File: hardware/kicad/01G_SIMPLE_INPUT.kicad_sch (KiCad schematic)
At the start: 2 parts

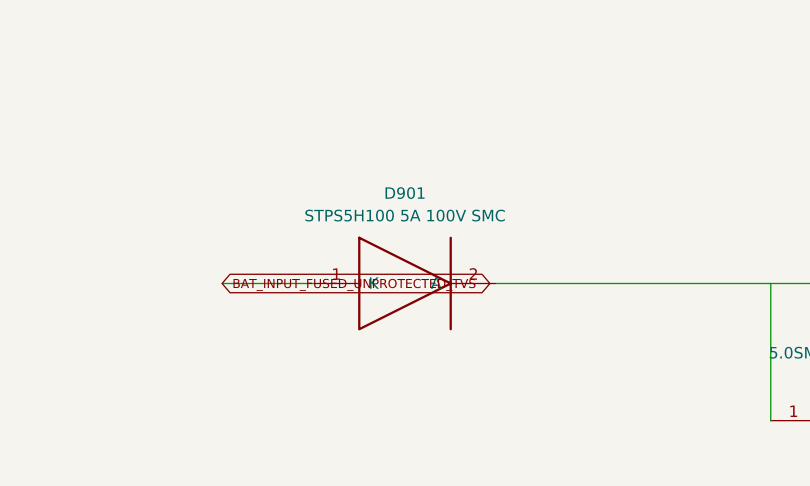
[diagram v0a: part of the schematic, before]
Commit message: fix(input): rotate series rectifier so BAT feeds anode and VIN is cathode
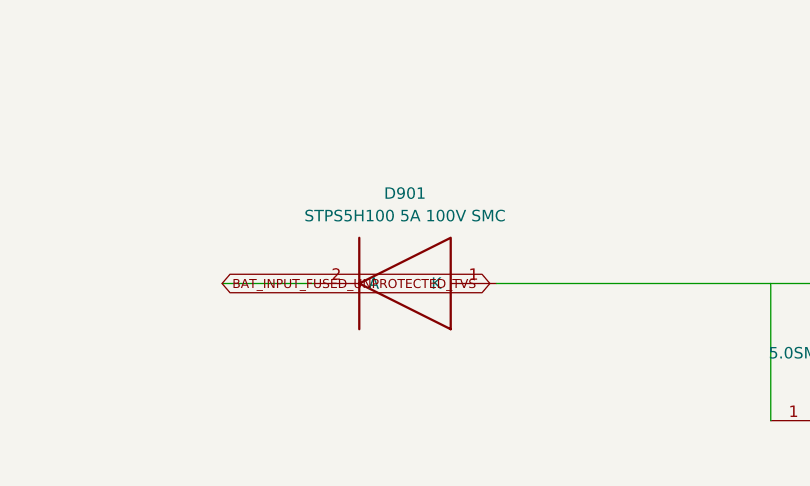
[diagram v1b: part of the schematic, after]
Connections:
- net BAT_INPUT_FUSED_UNPROTECTED_TVS: now also D901.2 (A); no longer D901.1 (K)
- net HV_PROTECTED_AFTER_EFUSE: now also D901.1 (K); no longer D901.2 (A)
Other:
- moved on the sheet: D901

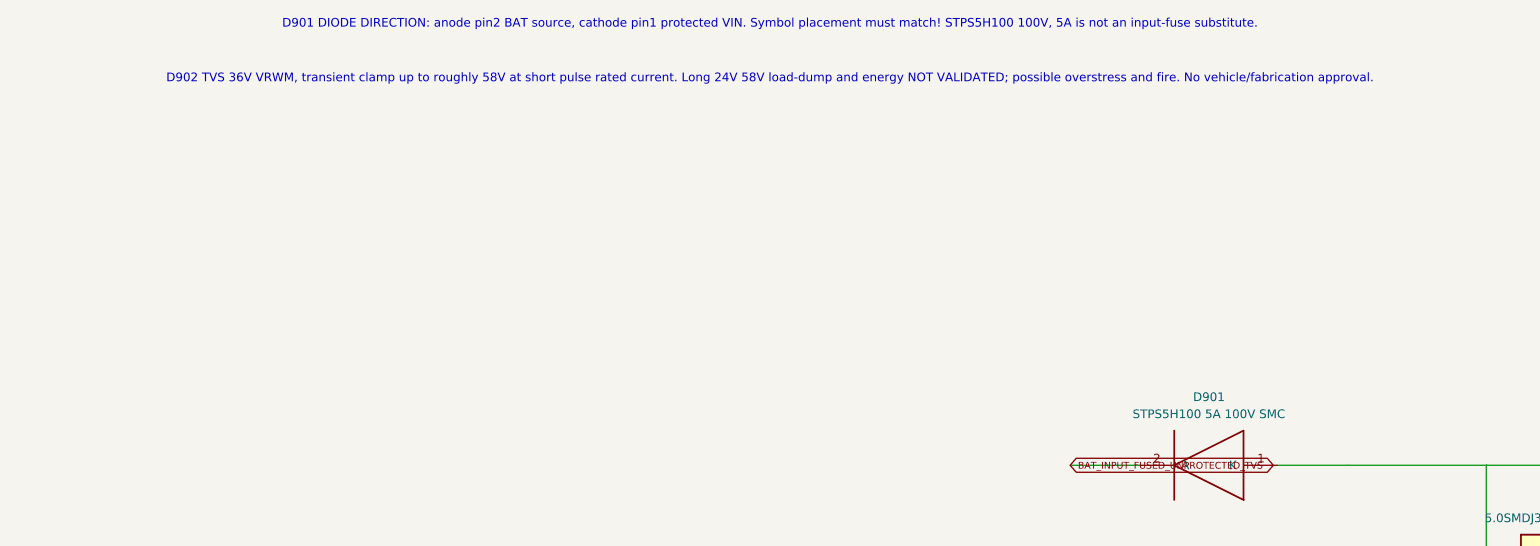
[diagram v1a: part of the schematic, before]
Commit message: hardware(input): correct D901 to footprint-compatible Comchip SS510C-HF 5A 100V SMC
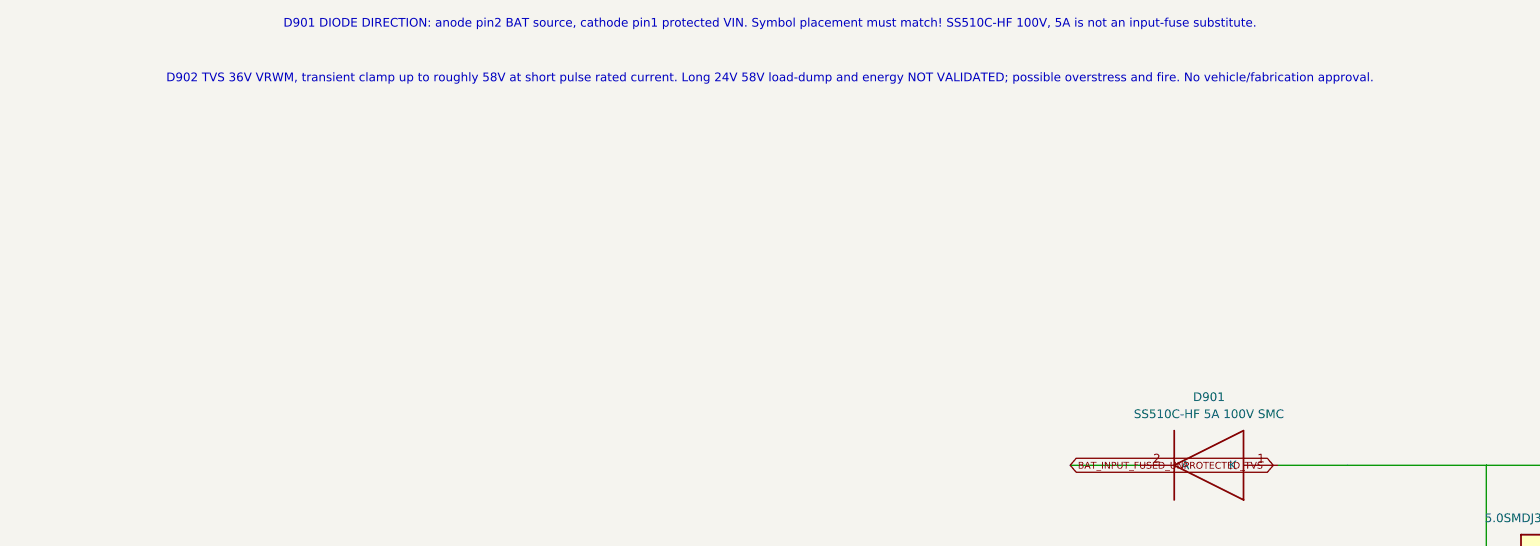
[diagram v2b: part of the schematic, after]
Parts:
- D901: value STPS5H100 5A 100V SMC -> SS510C-HF 5A 100V SMC; symbol TripTracer_V1:STPS5H100_SMC -> TripTracer_V1:SS510C_HF_SMC
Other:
- note added: "D901 DIODE DIRECTION: anode pin2 BAT source, cathode pin1 protected VIN. Symbol placement must match! SS510C-HF 100V, 5A is not an input-fuse substitute."
- note removed: "D901 DIODE DIRECTION: anode pin2 BAT source, cathode pin1 protected VIN. Symbol placement must match! STPS5H100 100V, 5A is not an input-fuse substitute."

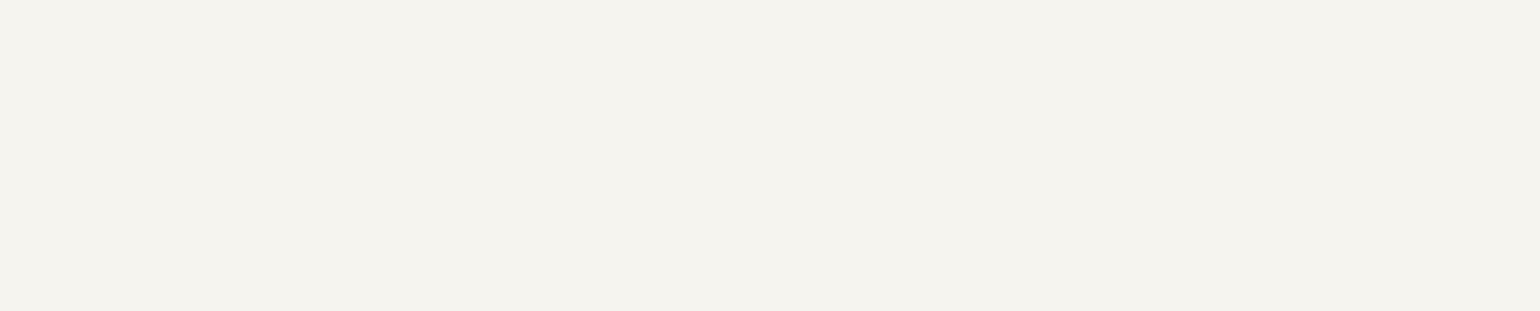
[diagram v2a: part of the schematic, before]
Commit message: hardware(input): expose independently externally fused BAT/ACC and ground on concrete 3-wire PCB pigtail connector
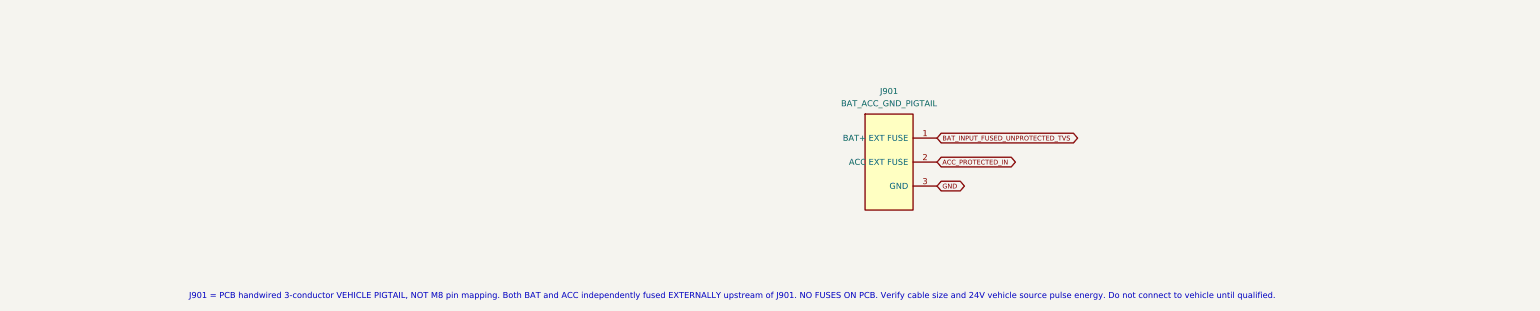
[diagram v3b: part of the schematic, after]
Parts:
- added J901: BAT_ACC_GND_PIGTAIL, Tripmaster:Vehicle_Pigtail_3Wire, symbol TripTracer_V1:POWER_HARNESS_3WIRE
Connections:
- net BAT_INPUT_FUSED_UNPROTECTED_TVS: now also J901.1 (BAT+ EXT FUSE)
- net GND: now also J901.3 (GND)
- new net ACC_PROTECTED_IN: J901.2 (ACC EXT FUSE)
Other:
- note added: "J901 = PCB handwired 3-conductor VEHICLE PIGTAIL, NOT M8 pin mapping. Both BAT and ACC independently fused EXTERNALLY upstream of J901. NO FUSES ON PCB. Verify cable size and 24V vehicle source pulse energy. Do not connect to vehicle until qualified."

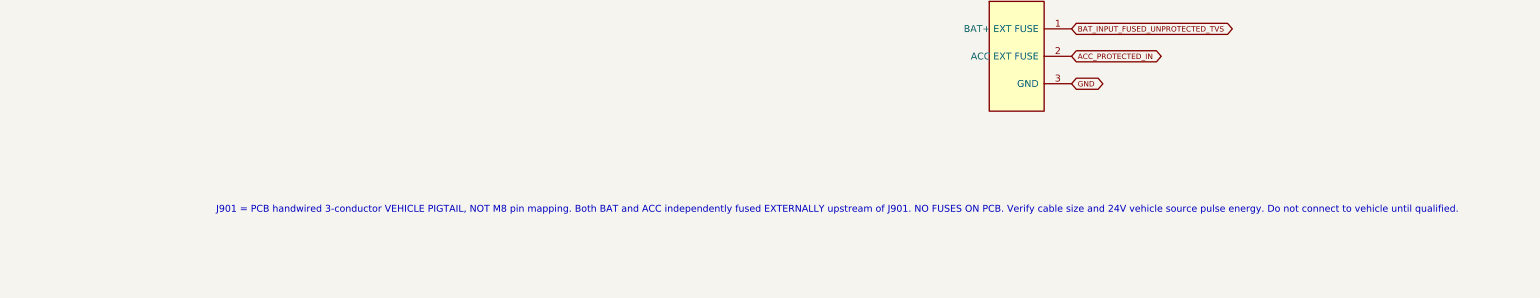
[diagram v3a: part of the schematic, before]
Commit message: fix(ERC): explicitly declare physically connected external BAT/GND and USB sources, not invented internal power
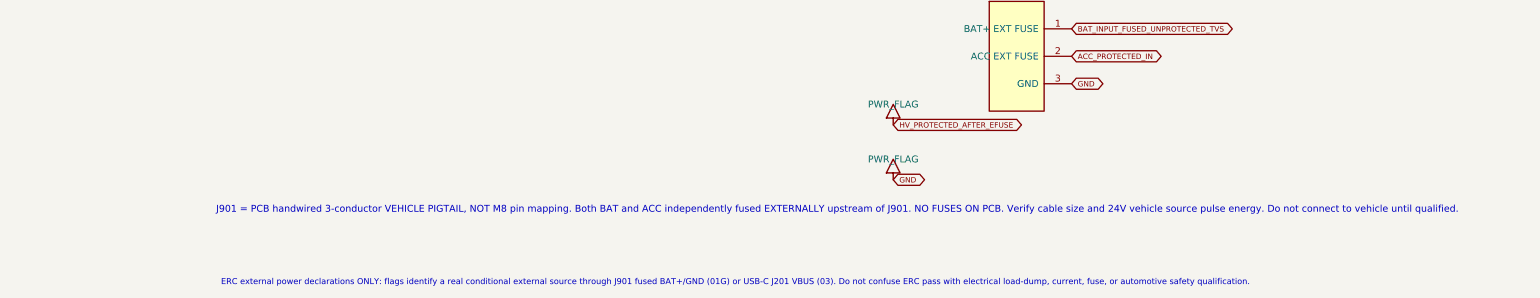
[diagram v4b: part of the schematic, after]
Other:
- note added: "ERC external power declarations ONLY: flags identify a real conditional external source through J901 fused BAT+/GND (01G) or USB-C J201 VBUS (03). Do not confuse ERC pass with electrical load-dump, current, fuse, or automotive safety qualification."
